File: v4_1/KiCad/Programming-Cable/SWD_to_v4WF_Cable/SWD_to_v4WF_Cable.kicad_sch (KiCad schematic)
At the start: 2 parts, among them J1 Conn_01x05, J2 Conn_02x05_Odd_Even

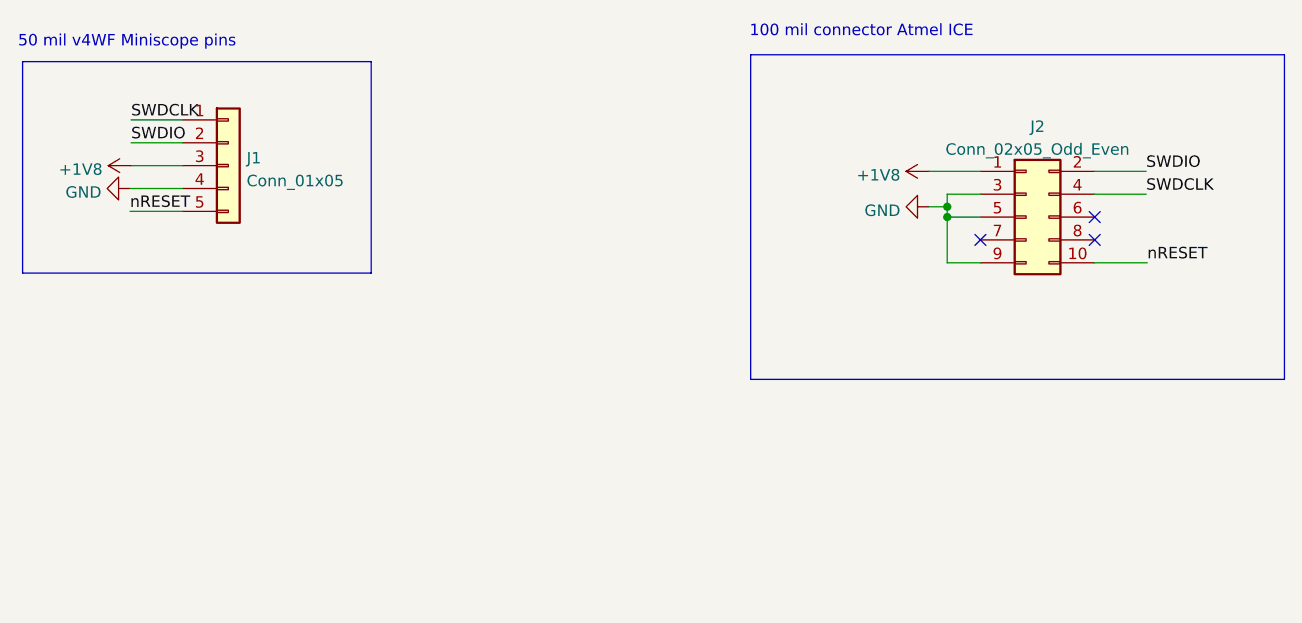
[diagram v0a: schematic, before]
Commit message: Modify and clean up swd programming PCB
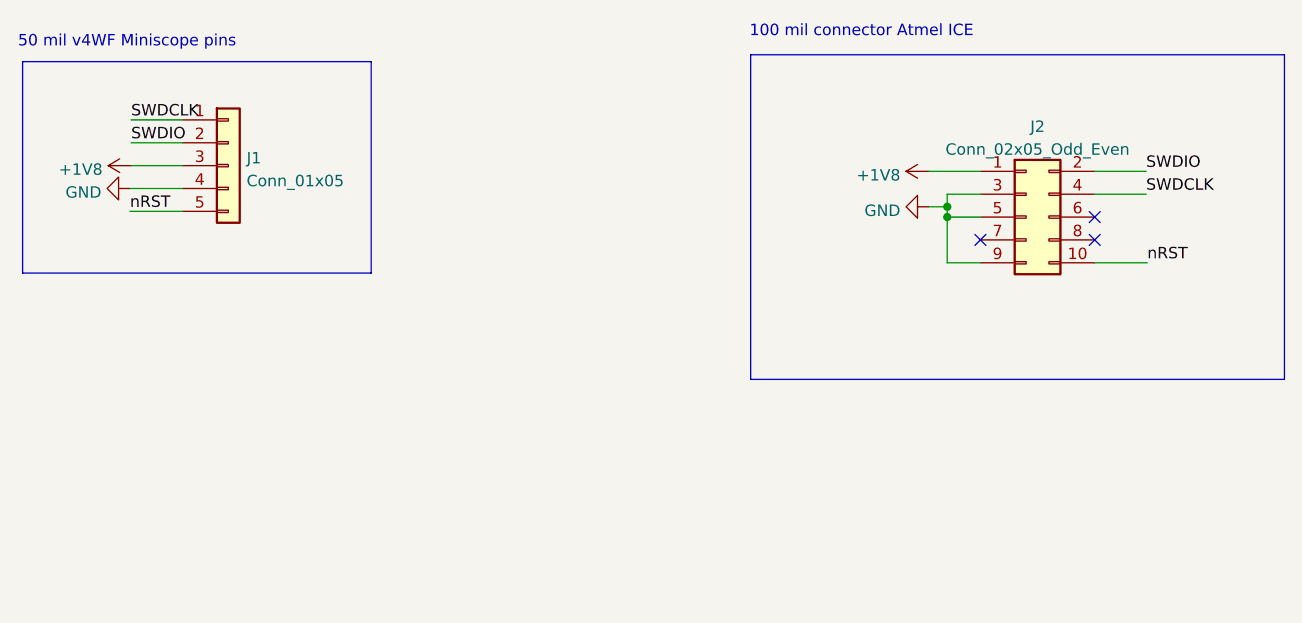
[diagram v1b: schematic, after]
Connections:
- net nRESET renamed nRST
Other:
- company: (none) -> Aharoni Lab
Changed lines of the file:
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@@
 (kicad_sch (version 20211123) (generator eeschema)
-  (paper "A4")
+  (paper "A")
+  (title_block
+    (date "2022-08-31")
+    (rev "0.1")
+    (company "Aharoni Lab")
+  )
   (junction (at 197.612 75.819) (diameter 0) (color 0 0 0 0)
   )
@@
     (effects (font (size 1.27 1.27)) (justify left bottom))
   )
-  (label "nRESET" (at 106.807 75.184 0)
+  (label "nRST" (at 106.807 75.184 0)
     (effects (font (size 1.27 1.27)) (justify left bottom))
   )
@@
     (effects (font (size 1.27 1.27)) (justify left bottom))
   )
-  (label "nRESET" (at 219.837 80.899 0)
+  (label "nRST" (at 219.837 80.899 0)
     (effects (font (size 1.27 1.27)) (justify left bottom))
   )

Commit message: Modification to the Programming cable PCB and firmware
- Corrected the footprint and layout of the programming cable PCB. Switched from a 100 mil pogo pin connector to the correct size (50 mil)
- Cleaned and built the firmware for flashing to the MCU
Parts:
- J1: footprint Connector_PinHeader_2.54mm:PinHeader_1x05_P2.54mm_Vertical -> Connector_PinSocket_1.00mm:PinSocket_1x05_P1.00mm_Vertical
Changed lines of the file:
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@@
       (effects (font (size 1.27 1.27)) (justify left))
     )
-    (property "Footprint" "Connector_PinHeader_2.54mm:PinHeader_1x05_P2.54mm_Vertical" (id 2) (at 117.729 70.104 0)
+    (property "Footprint" "Connector_PinSocket_1.00mm:PinSocket_1x05_P1.00mm_Vertical" (id 2) (at 117.729 70.104 0)
       (effects (font (size 1.27 1.27)) hide)
     )
@@
     )
     (path "/1848fb17-5179-40b4-bf82-55e641590875"
-      (reference "J1") (unit 1) (value "Conn_01x05") (footprint "Connector_PinHeader_2.54mm:PinHeader_1x05_P2.54mm_Vertical")
+      (reference "J1") (unit 1) (value "Conn_01x05") (footprint "Connector_PinSocket_1.00mm:PinSocket_1x05_P1.00mm_Vertical")
     )
     (path "/4632212f-13ce-4392-bc68-ccb9ba333770"

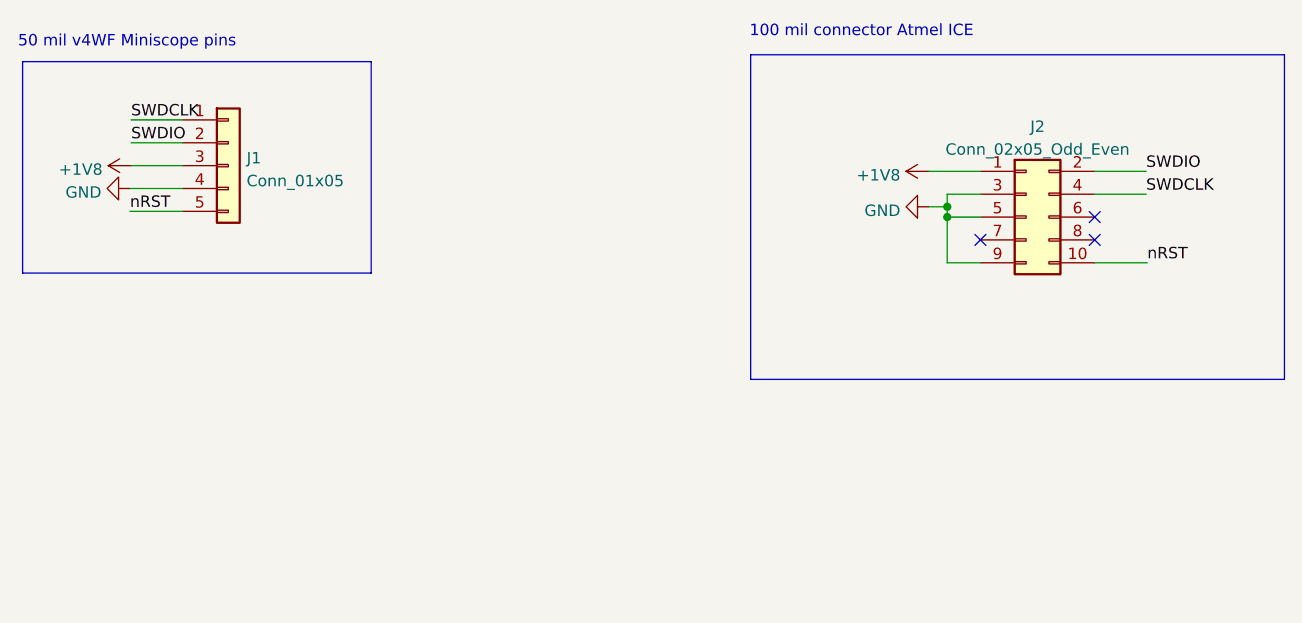
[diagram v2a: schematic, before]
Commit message: Updates to the project
- Added code to test the functionality of the v4 WF and validate the design
- Fixed a bug that left the EWL run continuously even if it was not recording. Now once the recording ends the EWL goes to sleep mode
- Modified the threshold for which the recording stops once the battery ADC reading reaches certain value
- Fixed a typo on the jupyter notebook name
- Fixed the programming cable by changing the target programming pins footprint
- Added a folder with a KiCAD project for the EWL cable
- For both things I generated new gerbers, which I checked using the gerber viewer
- Not uploaded to the repo due to size constrains: videos demonstrating that the Miniscope can record continuously for over 20 minutes

To do (in the short term):

- Add requirements to create a conda environment for easier use of the DAQ notebook
- Clean a bit more the code
- Add to the documentation the fix we applied to fix the bug that prevented the Miniscope to not run on Release mode
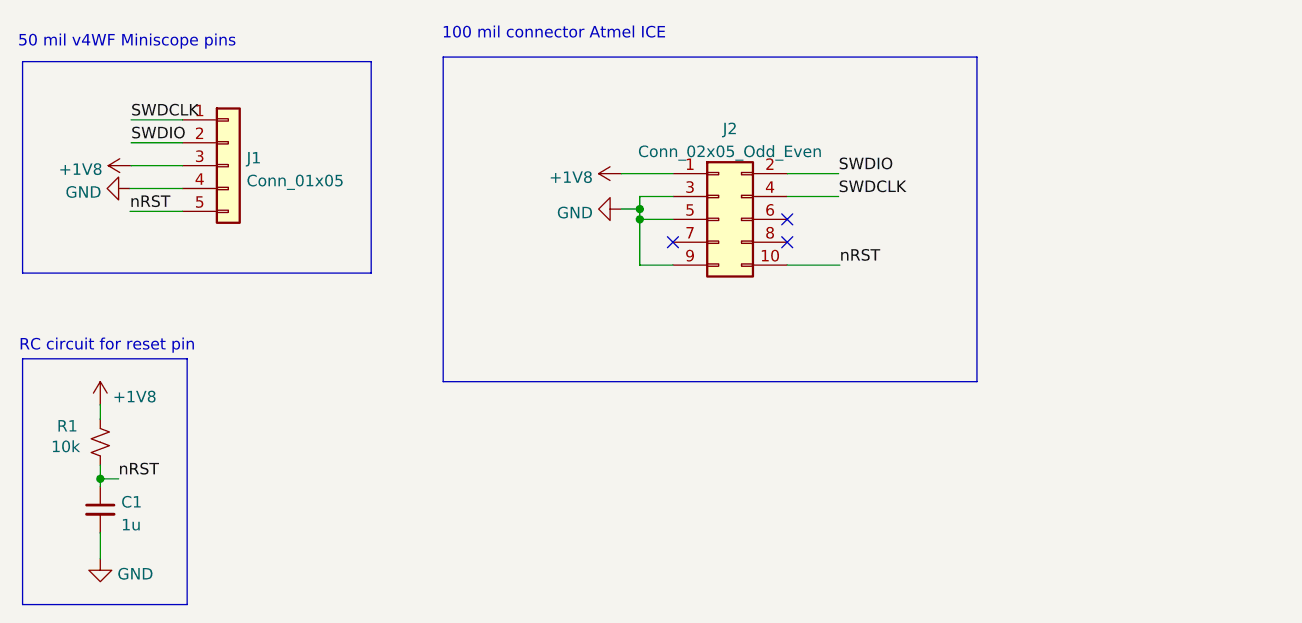
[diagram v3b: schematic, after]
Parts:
- added C1: 1u, Capacitor_SMD:C_0805_2012Metric_Pad1.18x1.45mm_HandSolder, symbol Device:C_Small
- added R1: 10k, Resistor_SMD:R_0805_2012Metric_Pad1.20x1.40mm_HandSolder, symbol Device:R_Small_US
- J1: footprint Connector_PinSocket_1.00mm:PinSocket_1x05_P1.00mm_Vertical -> Connector_PinSocket_1.27mm:PinSocket_1x05_P1.27mm_Vertical
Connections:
- net +1V8: now also R1.1
- net GND: now also C1.2
- net nRST: now also C1.1, R1.2
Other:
- note added: "RC circuit for reset pin"
- moved on the sheet: J2
